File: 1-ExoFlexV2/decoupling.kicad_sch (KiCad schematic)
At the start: 153 parts

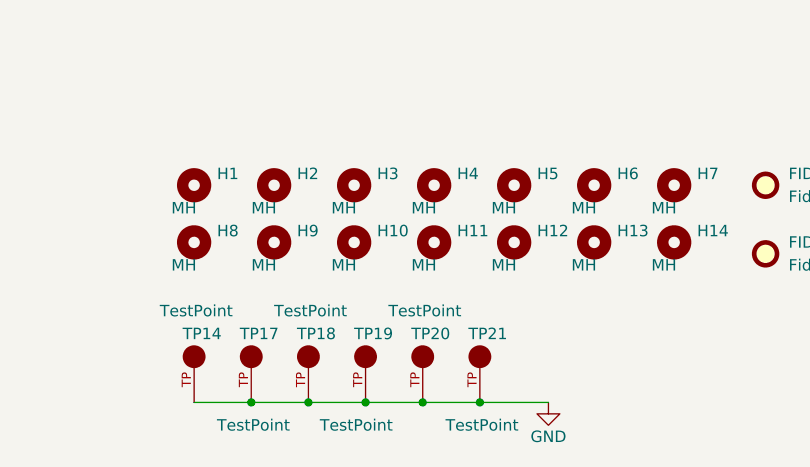
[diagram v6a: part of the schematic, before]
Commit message: Modification Schéma + Layout
- Ajout de RC potentiel entre les capteur de torque et l'ampli d'instru
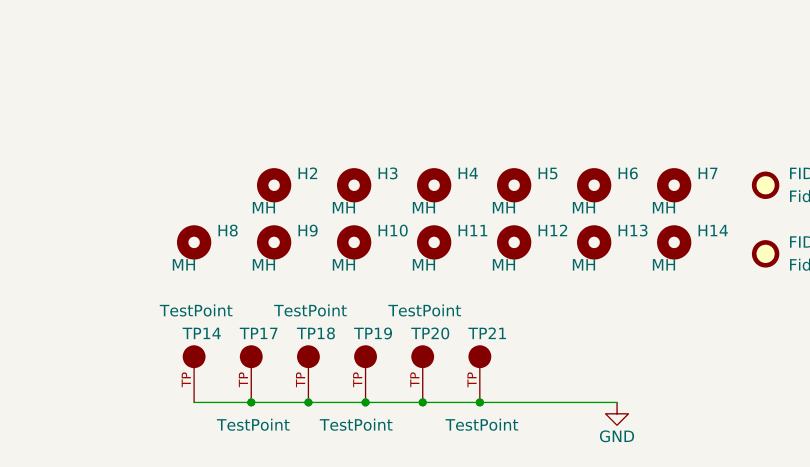
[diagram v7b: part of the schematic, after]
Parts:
- removed H1: MH, MountingHole:MountingHole_2.2mm_M2, symbol Mechanical:MountingHole
- H10, H11, H12, H13, H14, H2, H3, H4, H5, H6, H7, H8, H9: footprint MountingHole:MountingHole_2.2mm_M2 -> MountingHole:MountingHole_4.3mm_M4
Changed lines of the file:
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@@
     (stroke (width 0) (type default) (color 0 0 0 0))
   )
-  (wire (pts (xy 82.55 193.04) (xy 90.17 193.04))
+  (wire (pts (xy 82.55 193.04) (xy 97.79 193.04))
     (stroke (width 0) (type default) (color 0 0 0 0))
   )
@@
       (effects (font (size 1.27 1.27)) (justify left))
     )
-    (property "Footprint" "MountingHole:MountingHole_2.2mm_M2" (id 2) (at 95.25 175.26 0)
+    (property "Footprint" "MountingHole:MountingHole_4.3mm_M4" (id 2) (at 95.25 175.26 0)
       (effects (font (size 1.27 1.27)) hide)
     )
@@
       (effects (font (size 1.27 1.27)) (justify left))
     )
-    (property "Footprint" "MountingHole:MountingHole_2.2mm_M2" (id 2) (at 77.47 168.91 0)
+    (property "Footprint" "MountingHole:MountingHole_4.3mm_M4" (id 2) (at 77.47 168.91 0)
       (effects (font (size 1.27 1.27)) hide)
     )
@@
     (pin "2")
   )
-  (symbol (lib_id "power:GND") (at 90.17 193.04 0) (unit 1)
+  (symbol (lib_id "power:GND") (at 97.79 193.04 0) (unit 1)
     (in_bom yes) (on_board yes)
-    (property "Reference" "#PWR0519" (id 0) (at 90.17 199.39 0)
+    (property "Reference" "#PWR0519" (id 0) (at 97.79 199.39 0)
       (effects (font (size 1.27 1.27)) hide)
     )
-    (property "Value" "GND" (id 1) (at 90.17 196.85 0))
-    (property "Footprint" "" (id 2) (at 90.17 193.04 0)
+    (property "Value" "GND" (id 1) (at 97.79 196.85 0))
+    (property "Footprint" "" (id 2) (at 97.79 193.04 0)
       (effects (font (size 1.27 1.27)) hide)
     )
-    (property "Datasheet" "" (id 3) (at 90.17 193.04 0)
+    (property "Datasheet" "" (id 3) (at 97.79 193.04 0)
       (effects (font (size 1.27 1.27)) hide)
     )
@@
       (effects (font (size 1.27 1.27)) (justify left))
     )
-    (property "Footprint" "MountingHole:MountingHole_2.2mm_M2" (id 2) (at 86.36 175.26 0)
+    (property "Footprint" "MountingHole:MountingHole_4.3mm_M4" (id 2) (at 86.36 175.26 0)
       (effects (font (size 1.27 1.27)) hide)
     )
@@
       (effects (font (size 1.27 1.27)) (justify left))
     )
-    (property "Footprint" "MountingHole:MountingHole_2.2mm_M2" (id 2) (at 68.58 175.26 0)
+    (property "Footprint" "MountingHole:MountingHole_4.3mm_M4" (id 2) (at 68.58 175.26 0)
       (effects (font (size 1.27 1.27)) hide)
     )
@@
       (effects (font (size 1.27 1.27)) (justify left))
     )
-    (property "Footprint" "MountingHole:MountingHole_2.2mm_M2" (id 2) (at 59.69 168.91 0)
+    (property "Footprint" "MountingHole:MountingHole_4.3mm_M4" (id 2) (at 59.69 168.91 0)
       (effects (font (size 1.27 1.27)) hide)
     )
@@
       (effects (font (size 1.27 1.27)) (justify left))
     )
-    (property "Footprint" "MountingHole:MountingHole_2.2mm_M2" (id 2) (at 68.58 168.91 0)
+    (property "Footprint" "MountingHole:MountingHole_4.3mm_M4" (id 2) (at 68.58 168.91 0)
       (effects (font (size 1.27 1.27)) hide)
     )
@@
       (effects (font (size 1.27 1.27)) (justify left))
     )
-    (property "Footprint" "MountingHole:MountingHole_2.2mm_M2" (id 2) (at 86.36 168.91 0)
+    (property "Footprint" "MountingHole:MountingHole_4.3mm_M4" (id 2) (at 86.36 168.91 0)
       (effects (font (size 1.27 1.27)) hide)
     )
@@
       (effects (font (size 1.27 1.27)) (justify left))
     )
-    (property "Footprint" "MountingHole:MountingHole_2.2mm_M2" (id 2) (at 104.14 175.26 0)
+    (property "Footprint" "MountingHole:MountingHole_4.3mm_M4" (id 2) (at 104.14 175.26 0)
       (effects (font (size 1.27 1.27)) hide)
     )
@@
       (effects (font (size 1.27 1.27)) (justify left))
     )
-    (property "Footprint" "MountingHole:MountingHole_2.2mm_M2" (id 2) (at 77.47 175.26 0)
+    (property "Footprint" "MountingHole:MountingHole_4.3mm_M4" (id 2) (at 77.47 175.26 0)
       (effects (font (size 1.27 1.27)) hide)
     )
@@
       (effects (font (size 1.27 1.27)) (justify left))
     )
-    (property "Footprint" "MountingHole:MountingHole_2.2mm_M2" (id 2) (at 59.69 175.26 0)
+    (property "Footprint" "MountingHole:MountingHole_4.3mm_M4" (id 2) (at 59.69 175.26 0)
       (effects (font (size 1.27 1.27)) hide)
     )
@@
     (pin "2")
   )
-  (symbol (lib_id "Mechanical:MountingHole") (at 50.8 168.91 0) (unit 1)
-    (in_bom yes) (on_board yes)
-    (property "Reference" "H1" (id 0) (at 53.34 167.6399 0)
-      (effects (font (size 1.27 1.27)) (justify left))
-    )
-    (property "Value" "MH" (id 1) (at 48.26 171.45 0)
-      (effects (font (size 1.27 1.27)) (justify left))
-    )
-    (property "Footprint" "MountingHole:MountingHole_2.2mm_M2" (id 2) (at 50.8 168.91 0)
-      (effects (font (size 1.27 1.27)) hide)
-    )
-    (property "Datasheet" "~" (id 3) (at 50.8 168.91 0)
-      (effects (font (size 1.27 1.27)) hide)
-    )
-  )
   (symbol (lib_id "Device:C") (at 147.32 41.91 0) (unit 1)
     (in_bom yes) (on_board yes)
@@
       (effects (font (size 1.27 1.27)) (justify left))
     )
-    (property "Footprint" "MountingHole:MountingHole_2.2mm_M2" (id 2) (at 50.8 175.26 0)
+    (property "Footprint" "MountingHole:MountingHole_4.3mm_M4" (id 2) (at 50.8 175.26 0)
       (effects (font (size 1.27 1.27)) hide)
     )
@@
       (effects (font (size 1.27 1.27)) (justify left))
     )
-    (property "Footprint" "MountingHole:MountingHole_2.2mm_M2" (id 2) (at 104.14 168.91 0)
+    (property "Footprint" "MountingHole:MountingHole_4.3mm_M4" (id 2) (at 104.14 168.91 0)
       (effects (font (size 1.27 1.27)) hide)
     )
@@
       (effects (font (size 1.27 1.27)) (justify left))
     )
-    (property "Footprint" "MountingHole:MountingHole_2.2mm_M2" (id 2) (at 95.25 168.91 0)
+    (property "Footprint" "MountingHole:MountingHole_4.3mm_M4" (id 2) (at 95.25 168.91 0)
       (effects (font (size 1.27 1.27)) hide)
     )
